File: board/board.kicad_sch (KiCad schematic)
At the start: 49 parts, among them J1 UART, J2 USB_B, Q2 Q_NPN_BEC, SW1 SW_SPST, SW2 SW_SPST, SW4 SW_SPST, U1 4040, U2 NE555D, U3 4040, U4 LM741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

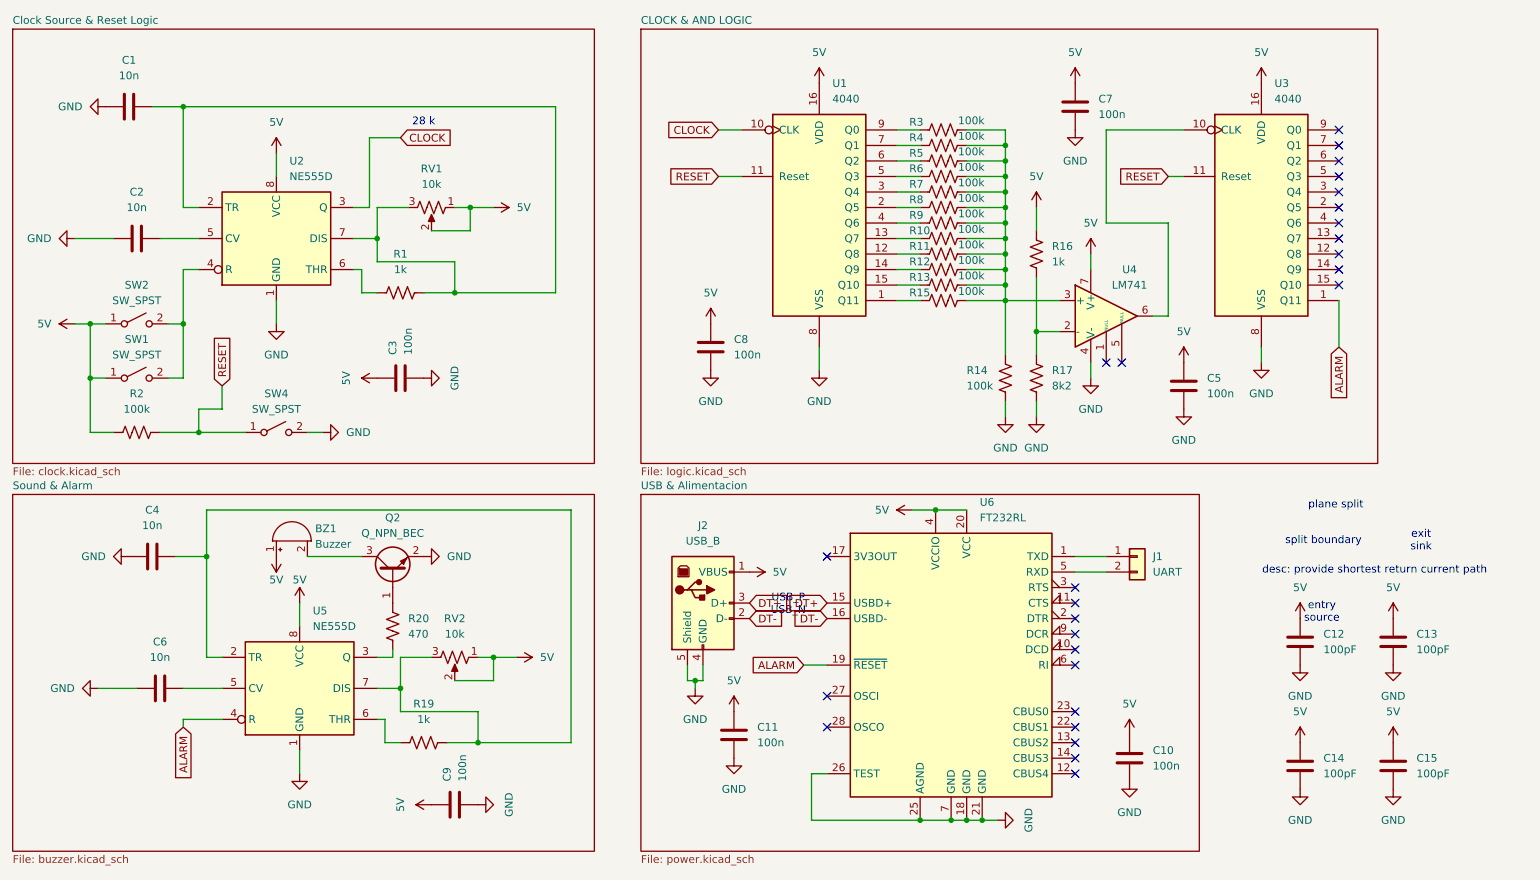
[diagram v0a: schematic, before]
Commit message: add: Hierarchical Sheets
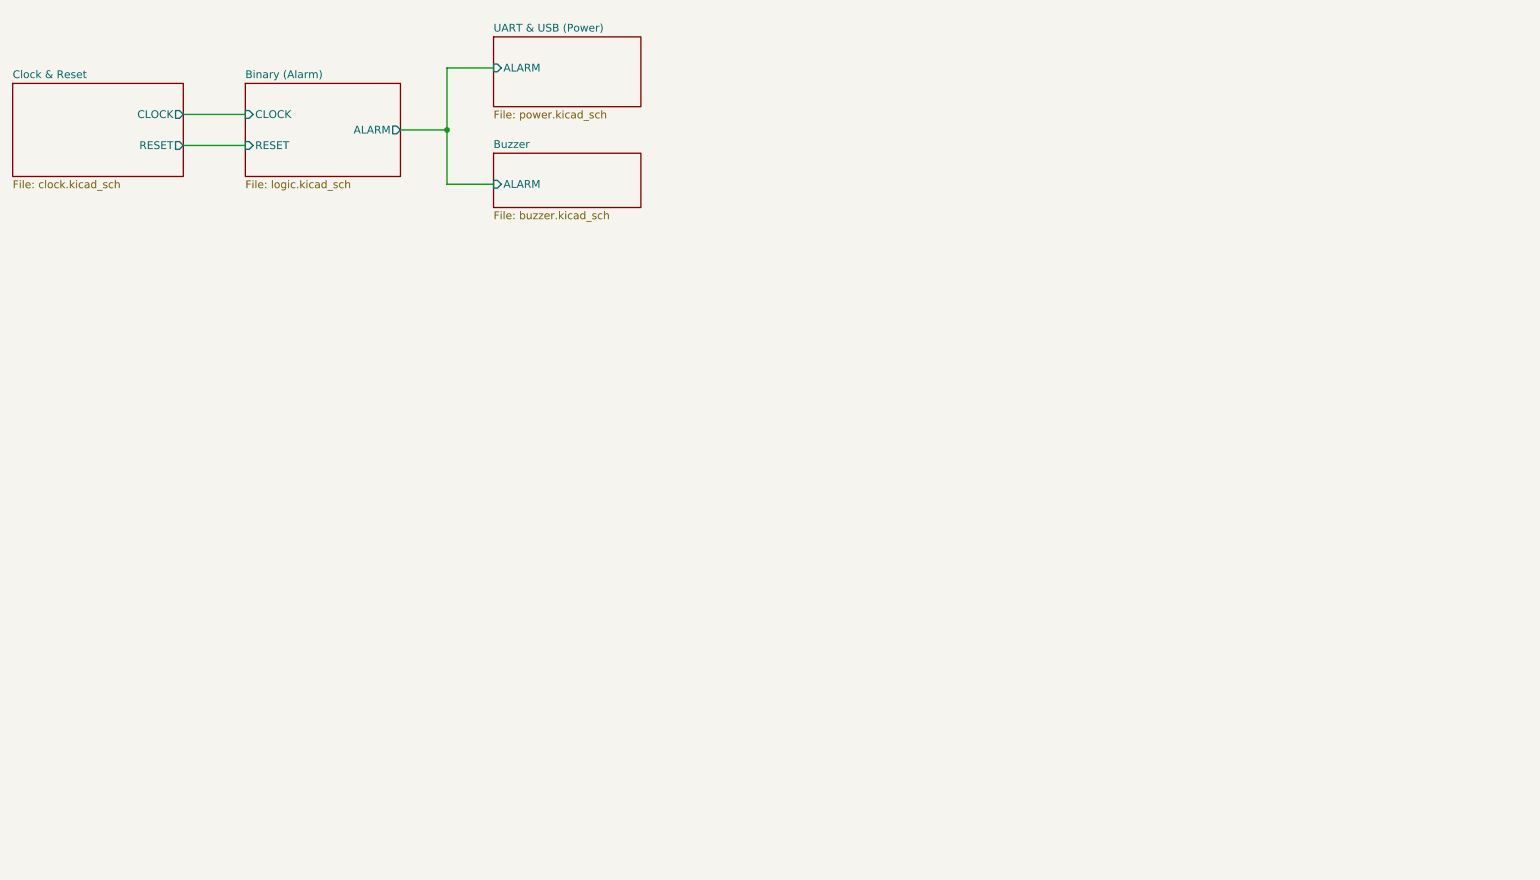
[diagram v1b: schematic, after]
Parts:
- removed BZ1: Buzzer, Buzzer_Beeper:MagneticBuzzer_PUI_AT-0927-TT-6-R, symbol Device:Buzzer
- removed C1, C2, C4, C6: 10n, Capacitor_SMD:C_0603_1608Metric, symbol Device:C
- removed C10, C11, C3, C5, C7, C8, C9: 100n, Capacitor_SMD:C_0603_1608Metric, symbol Device:C
- removed C12, C13, C14, C15: 100pF, Capacitor_SMD:C_0201_0603Metric, symbol Device:C
- removed J1: UART, Connector_PinSocket_2.54mm:PinSocket_1x02_P2.54mm_Vertical, symbol Connector_Generic:Conn_01x02
- removed J2: USB_B, Connector_USB:USB_Mini-B_Lumberg_2486_01_Horizontal, symbol Connector:USB_B
- removed Q2: Q_NPN_BEC, Package_TO_SOT_SMD:SOT-23, symbol Transistor_BJT:Q_NPN_BEC
- removed R1, R16, R19: 1k, Resistor_SMD:R_0603_1608Metric, symbol Device:R_US
- removed R10, R11, R12, R13, R14, R15, R2, R3, R4, R5, R6, R7, R8, R9: 100k, Resistor_SMD:R_0603_1608Metric, symbol Device:R_US
- removed R17: 8k2, Resistor_SMD:R_0603_1608Metric, symbol Device:R_US
- removed R20: 470, Resistor_SMD:R_0603_1608Metric, symbol Device:R_US
- removed RV1, RV2: 10k, Potentiometer_THT:Potentiometer_Piher_PT-6-V_Vertical, symbol Device:R_Potentiometer_US
- removed SW1, SW2, SW4: SW_SPST, Button_Switch_THT:SW_PUSH_6mm_H4.3mm, symbol Switch:SW_SPST
- removed U1, U3: 4040, Package_SO:SO-16_3.9x9.9mm_P1.27mm, symbol 4xxx:4040
- removed U2, U5: NE555D, Package_SO:SOIC-8_3.9x4.9mm_P1.27mm, symbol Timer:NE555D
- removed U4: LM741, Package_SO:SOIC-8_3.9x4.9mm_P1.27mm, symbol Amplifier_Operational:LM741
- removed U6: FT232RL, Package_SO:SSOP-28_5.3x10.2mm_P0.65mm, symbol Interface_USB:FT232RL
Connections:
- no-connect marks 27 -> 0
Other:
- sheet CLOCK & AND LOGIC renamed Binary (Alarm)
- sheet Clock Source & Reset Logic renamed Clock & Reset
- sheet Sound & Alarm renamed Buzzer
- sheet USB & Alimentacion renamed UART & USB (Power)
- sheet Binary (Alarm) ports: added ALARM, CLOCK, RESET; removed none
- sheet Buzzer ports: added ALARM; removed none
- sheet Clock & Reset ports: added CLOCK, RESET; removed none
- sheet UART & USB (Power) ports: added ALARM; removed none
- note removed: "28 k"
- note removed: "USB_P USB_N"
- note removed: "desc: provide shortest return current path"
- note removed: "entry source"
- note removed: "exit sink"
- note removed: "plane split"
- note removed: "split boundary"

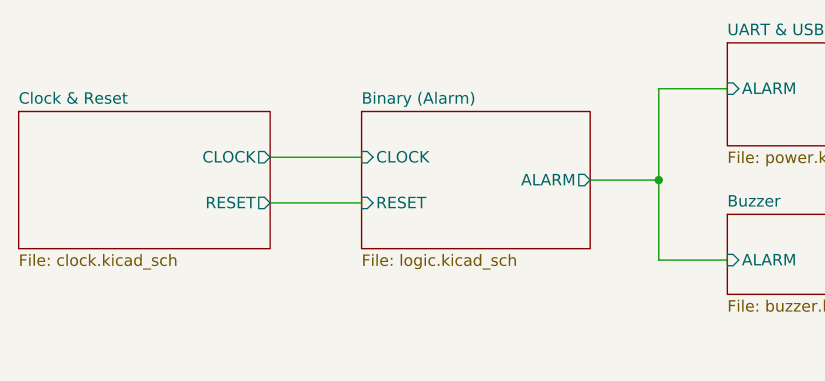
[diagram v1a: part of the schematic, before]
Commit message: add: Mounting holes, box comments
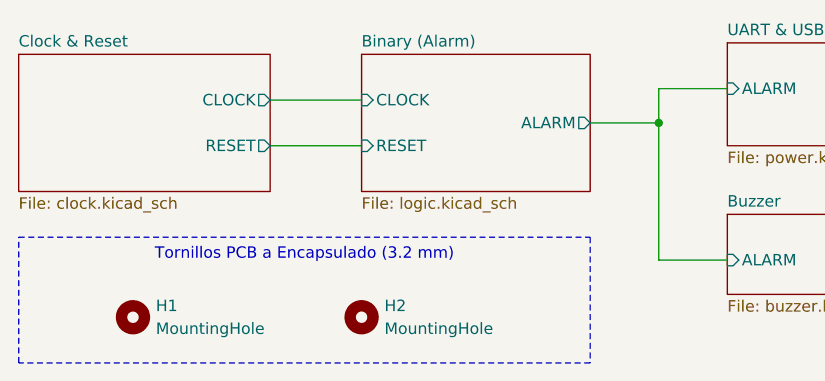
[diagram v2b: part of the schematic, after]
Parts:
- added H1, H2: MountingHole, MountingHole:MountingHole_3.2mm_M3, symbol Mechanical:MountingHole
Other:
- company: UCU -> Universidad Catolica del Uruguay
- title: Esquematico Toma Mate -> Esquematico Alarma Mate
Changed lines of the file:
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@@
 	(paper "User" 139.7 101.6)
 	(title_block
-		(title "Esquematico Toma Mate")
+		(title "Esquematico Alarma Mate")
 		(date "2025-04-26")
-		(company "UCU")
-		(comment 1 "Toma mate")
+		(company "Universidad Catolica del Uruguay")
+		(comment 1 "Alarma cada 5 minutos")
+	)
+	(text_box "Tornillos PCB a Encapsulado (3.2 mm)\n"
+		(exclude_from_sim no)
+		(at 19.05 41.91 0)
+		(size 63.5 13.97)
+		(margins 0.9525 0.9525 0.9525 0.9525)
+		(stroke
+			(width 0)
+			(type dot)
+		)
+		(fill
+			(type none)
+		)
+		(effects
+			(font
+				(size 1.27 1.27)
+			)
+			(justify top)
+		)
 	)
 	(junction
-		(at 90.17 35.56)
+		(at 90.17 29.21)
 		(diameter 0)
 		(color 0 0 0 0)
@@
 	(wire
 		(pts
-			(xy 46.99 33.02) (xy 57.15 33.02)
-		)
-		(stroke
-			(width 0)
-			(type default)
-		)
-	)
-	(wire
-		(pts
-			(xy 46.99 38.1) (xy 57.15 38.1)
+			(xy 46.99 26.67) (xy 57.15 26.67)
+		)
+		(stroke
+			(width 0)
+			(type default)
+		)
+	)
+	(wire
+		(pts
+			(xy 46.99 31.75) (xy 57.15 31.75)
+		)
+		(stroke
+			(width 0)
+			(type default)
+		)
+	)
+	(wire
+		(pts
+			(xy 90.17 29.21) (xy 90.17 25.4)
 		)
 		(stroke
@@
 	(wire
 		(pts
-			(xy 90.17 35.56) (xy 90.17 25.4)
-		)
-		(stroke
-			(width 0)
-			(type default)
-		)
-	)
-	(wire
-		(pts
-			(xy 90.17 44.45) (xy 90.17 35.56)
-		)
-		(stroke
-			(width 0)
-			(type default)
-		)
-	)
-	(wire
-		(pts
-			(xy 82.55 35.56) (xy 90.17 35.56)
-		)
-		(stroke
-			(width 0)
-			(type default)
+			(xy 90.17 29.21) (xy 90.17 44.45)
+		)
+		(stroke
+			(width 0)
+			(type default)
+		)
+	)
+	(wire
+		(pts
+			(xy 82.55 29.21) (xy 90.17 29.21)
+		)
+		(stroke
+			(width 0)
+			(type default)
+		)
+	)
+	(symbol
+		(lib_id "Mechanical:MountingHole")
+		(at 57.15 50.8 0)
+		(unit 1)
+		(exclude_from_sim no)
+		(in_bom no)
+		(on_board yes)
+		(dnp no)
+		(fields_autoplaced yes)
+		(property "Reference" "H2"
+			(at 59.69 49.5299 0)
+			(effects
+				(font
+					(size 1.27 1.27)
+				)
+				(justify left)
+			)
+		)
+		(property "Value" "MountingHole"
+			(at 59.69 52.0699 0)
+			(effects
+				(font
+					(size 1.27 1.27)
+				)
+				(justify left)
+			)
+		)
+		(property "Footprint" "MountingHole:MountingHole_3.2mm_M3"
+			(at 57.15 50.8 0)
+			(effects
+				(font
+					(size 1.27 1.27)
+				)
+				(hide yes)
+			)
+		)
+		(property "Datasheet" "~"
+			(at 57.15 50.8 0)
+			(effects
+				(font
+					(size 1.27 1.27)
+				)
+				(hide yes)
+			)
+		)
+		(property "Description" "Mounting Hole without connection"
+			(at 57.15 50.8 0)
+			(effects
+				(font
+					(size 1.27 1.27)
+				)
+				(hide yes)
+			)
+		)
+		(instances
+			(project "board"
+				(path "/b7e46b49-ef9f-4f28-8032-5d189d1635e8"
+					(reference "H2")
+					(unit 1)
+				)
+			)
+		)
+	)
+	(symbol
+		(lib_id "Mechanical:MountingHole")
+		(at 31.75 50.8 0)
+		(unit 1)
+		(exclude_from_sim no)
+		(in_bom no)
+		(on_board yes)
+		(dnp no)
+		(fields_autoplaced yes)
+		(property "Reference" "H1"
+			(at 34.29 49.5299 0)
+			(effects
+				(font
+					(size 1.27 1.27)
+				)
+				(justify left)
+			)
+		)
+		(property "Value" "MountingHole"
+			(at 34.29 52.0699 0)
+			(effects
+				(font
+					(size 1.27 1.27)
+				)
+				(justify left)
+			)
+		)
+		(property "Footprint" "MountingHole:MountingHole_3.2mm_M3"
+			(at 31.75 50.8 0)
+			(effects
+				(font
+					(size 1.27 1.27)
+				)
+				(hide yes)
+			)
+		)
+		(property "Datasheet" "~"
+			(at 31.75 50.8 0)
+			(effects
+				(font
+					(size 1.27 1.27)
+				)
+				(hide yes)
+			)
+		)
+		(property "Description" "Mounting Hole without connection"
+			(at 31.75 50.8 0)
+			(effects
+				(font
+					(size 1.27 1.27)
+				)
+				(hide yes)
+			)
+		)
+		(instances
+			(project ""
+				(path "/b7e46b49-ef9f-4f28-8032-5d189d1635e8"
+					(reference "H1")
+					(unit 1)
+				)
+			)
 		)
 	)
@@
 	)
 	(sheet
-		(at 19.05 27.94)
+		(at 19.05 21.59)
 		(size 27.94 15.24)
 		(exclude_from_sim no)
@@
 		)
 		(property "Sheetname" "Clock & Reset"
-			(at 19.05 27.2284 0)
+			(at 19.05 20.8784 0)
 			(effects
 				(font
@@
 		)
 		(property "Sheetfile" "clock.kicad_sch"
-			(at 19.05 43.7646 0)
+			(at 19.05 37.4146 0)
 			(effects
 				(font
@@
 		)
 		(pin "CLOCK" output
-			(at 46.99 33.02 0)
+			(at 46.99 26.67 0)
 			(effects
 				(font
@@
 		)
 		(pin "RESET" output
-			(at 46.99 38.1 0)
+			(at 46.99 31.75 0)
 			(effects
 				(font
@@
 	)
 	(sheet
-		(at 57.15 27.94)
+		(at 57.15 21.59)
 		(size 25.4 15.24)
 		(exclude_from_sim no)
@@
 		)
 		(property "Sheetname" "Binary (Alarm)"
-			(at 57.15 27.2284 0)
+			(at 57.15 20.8784 0)
 			(effects
 				(font
@@
 		)
 		(property "Sheetfile" "logic.kicad_sch"
-			(at 57.15 43.7646 0)
+			(at 57.15 37.4146 0)
 			(effects
 				(font
@@
 		)
 		(pin "ALARM" output
-			(at 82.55 35.56 0)
+			(at 82.55 29.21 0)
 			(effects
 				(font
@@
 		)
 		(pin "CLOCK" input
-			(at 57.15 33.02 180)
+			(at 57.15 26.67 180)
 			(effects
 				(font
@@
 		)
 		(pin "RESET" input
-			(at 57.15 38.1 180)
-			(effects
-				(font
+			(at 57.15 31.75 180)
+			(effects
+				(font

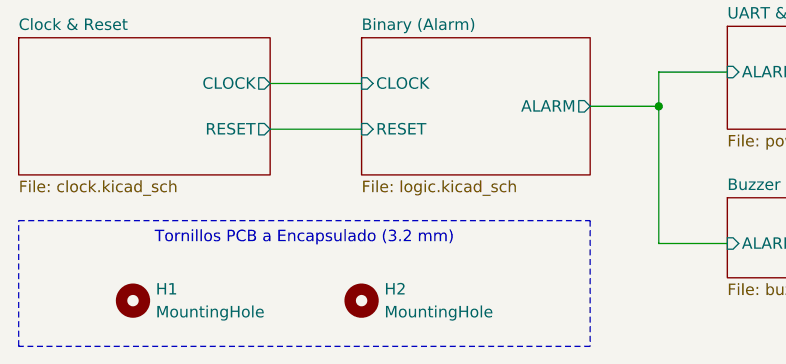
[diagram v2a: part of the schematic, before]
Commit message: add: 9mm 3d push btn, VCC GND pins (battery)
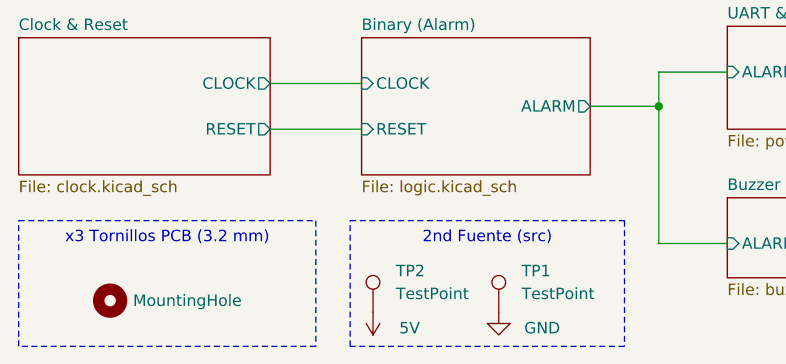
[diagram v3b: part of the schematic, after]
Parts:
- removed H2: MountingHole, MountingHole:MountingHole_3.2mm_M3, symbol Mechanical:MountingHole
- added TP1, TP2: TestPoint, TestPoint:TestPoint_THTPad_2.0x2.0mm_Drill1.0mm, symbol Connector:TestPoint
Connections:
- new net 5V: TP2.1
- new net GND: TP1.1

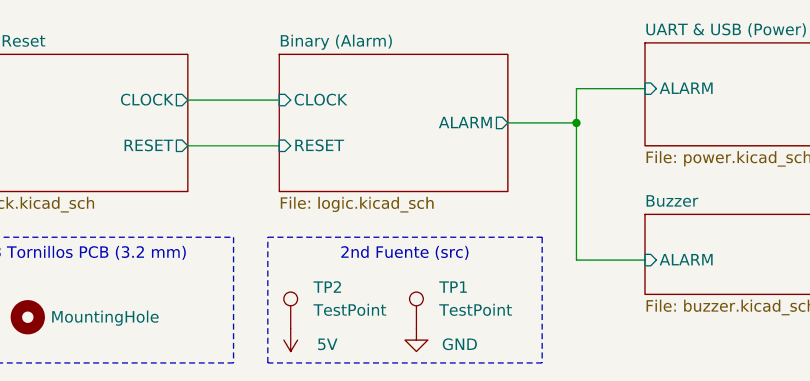
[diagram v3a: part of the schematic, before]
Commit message: add: rectangle TIP GNS
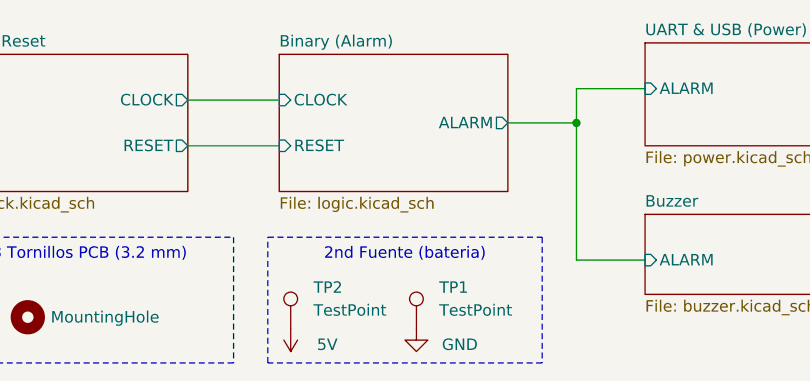
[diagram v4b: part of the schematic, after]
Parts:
- TP2: footprint TestPoint:TestPoint_THTPad_2.0x2.0mm_Drill1.0mm -> TestPoint:TestPoint_THTPad_D2.0mm_Drill1.0mm
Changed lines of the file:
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@@
 		(comment 1 "Alarma cada 5 minutos")
 	)
-	(text_box "2nd Fuente (src)"
+	(text_box "2nd Fuente (bateria)"
 		(exclude_from_sim no)
 		(at 55.88 41.91 0)
@@
 			)
 		)
-		(property "Footprint" "TestPoint:TestPoint_THTPad_2.0x2.0mm_Drill1.0mm"
+		(property "Footprint" "TestPoint:TestPoint_THTPad_D2.0mm_Drill1.0mm"
 			(at 63.5 52.07 0)
 			(effects
